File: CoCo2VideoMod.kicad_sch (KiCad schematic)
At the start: 22 parts, among them J1 Conn_01x05, J2 Conn_01x03

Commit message: circuit diagramm completed
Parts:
- added C1: 100n, symbol Device:C
- added C?: 1u, symbol Device:C
- added J3: Conn_01x06, symbol Connector_Generic:Conn_01x06
- added Q1, Q3: BC547, Package_TO_SOT_THT:TO-92_Inline, symbol Transistor_BJT:BC547
- added Q2: BC557, Package_TO_SOT_THT:TO-92_Inline, symbol Transistor_BJT:BC557
- added R? (x2): 75R, symbol Device:R
- added R? (x2): 470R, symbol Device:R
- added R?: 4k7, symbol Device:R
- added R?: 330R, symbol Device:R
- added R?: 10k, symbol Device:R
- added R?: 680R, symbol Device:R
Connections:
- net +5V: now also C1.1, Q1.1 (C), Q3.1 (C), R?.2, R?.2
- net Audio out: now also J3.1 (Pin_1)
- net GND: now also J3.3 (Pin_3), J3.4 (Pin_4), R?.1, R?.1, R?.1, R?.1
- net Luma: now also C?.2, J3.5 (Pin_5), R?.2
- net V_comp: now also J3.2 (Pin_2)
- net at R?.2, U?.8 (Co): now also Q1.2 (B)
- new net: Q1.3 (E), R?.1, R?.2
- new net: Q3.3 (E), R?.1, R?.2
- new net: C1.2, Q2.3 (E), R?.1
- new net: C?.1, Q2.2 (B), R?.1, R?.2
- new net: Q2.1 (C), Q3.2 (B), R?.2
- new net Chroma: J3.6 (Pin_6), R?.2
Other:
- moved on the sheet: C?, D?, J1, J2, L?, Q?, R?, U?

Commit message: footprint annotation
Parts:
- removed C?: 100u, symbol Device:C
- added C2: 220u, Capacitor_THT:CP_Radial_D6.3mm_P2.50mm, symbol Device:C_Polarized
- C1: value 100n -> 100p; footprint (none) -> Capacitor_THT:C_Disc_D4.7mm_W2.5mm_P5.00mm
- C3, C8: renamed from C?; footprint (none) -> Capacitor_THT:C_Rect_L7.0mm_W3.5mm_P5.00mm
- C4, C5, C7: renamed from C?; footprint (none) -> Capacitor_THT:C_Rect_L9.0mm_W4.2mm_P7.50mm_MKT
- C6: renamed from C?; footprint (none) -> Capacitor_THT:C_Rect_L7.0mm_W4.5mm_P5.00mm
- D1: renamed from D?; footprint (none) -> Diode_THT:D_DO-35_SOD27_P2.54mm_Vertical_AnodeUp
- J1: footprint (none) -> Connector_PinHeader_2.54mm:PinHeader_1x05_P2.54mm_Vertical
- J2: footprint (none) -> Connector_PinHeader_2.54mm:PinHeader_1x03_P2.54mm_Vertical
- J3: value Conn_01x06 -> Mini DIN 6p; footprint (none) -> Custom_Footprints:Connector_Mini-DIN_Female_6Pin_2rows
- L1: renamed from L?; footprint (none) -> Inductor_THT:L_Axial_L6.6mm_D2.7mm_P10.16mm_Horizontal_Vishay_IM-2
- R1, R10, R11, R12, R13, R14, R15, R16, R17, R2, R3, R4, R5, R6, R7, R8, R9: renamed from R?; footprint (none) -> Resistor_THT:R_Axial_DIN0207_L6.3mm_D2.5mm_P10.16mm_Horizontal
- U1: renamed from U?; footprint (none) -> Package_DIP:DIP-14_W7.62mm
- gave numbers to parts that had none: 2
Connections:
- net +5V: now also C2.1
- net GND: now also C2.2

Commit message: mid routing
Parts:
- removed J3: Mini DIN 6p, Custom_Footprints:Connector_Mini-DIN_Female_6Pin_2rows, symbol Connector_Generic:Conn_01x06
- added J3: Conn_01x07, Custom_Footprints:Connector_Mini-DIN_Female_6Pin_2rows, symbol Connector_Generic:Conn_01x07
- C1: footprint Capacitor_THT:C_Disc_D4.7mm_W2.5mm_P5.00mm -> Capacitor_THT:C_Disc_D3.0mm_W2.0mm_P2.50mm
- R1, R10, R11, R12, R13, R14, R15, R16, R17, R2, R3, R4, R5, R6, R7, R8, R9: footprint Resistor_THT:R_Axial_DIN0207_L6.3mm_D2.5mm_P10.16mm_Horizontal -> Resistor_THT:R_Axial_DIN0207_L6.3mm_D2.5mm_P2.54mm_Vertical
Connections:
- net Audio out: now also J3.1 (Pin_1)
- net Chroma: now also J3.6 (Pin_6)
- net GND: now also J3.3 (Pin_3), J3.4 (Pin_4), J3.7 (Pin_7)
- net Luma: now also J3.5 (Pin_5)
- net V_comp: now also J3.2 (Pin_2)

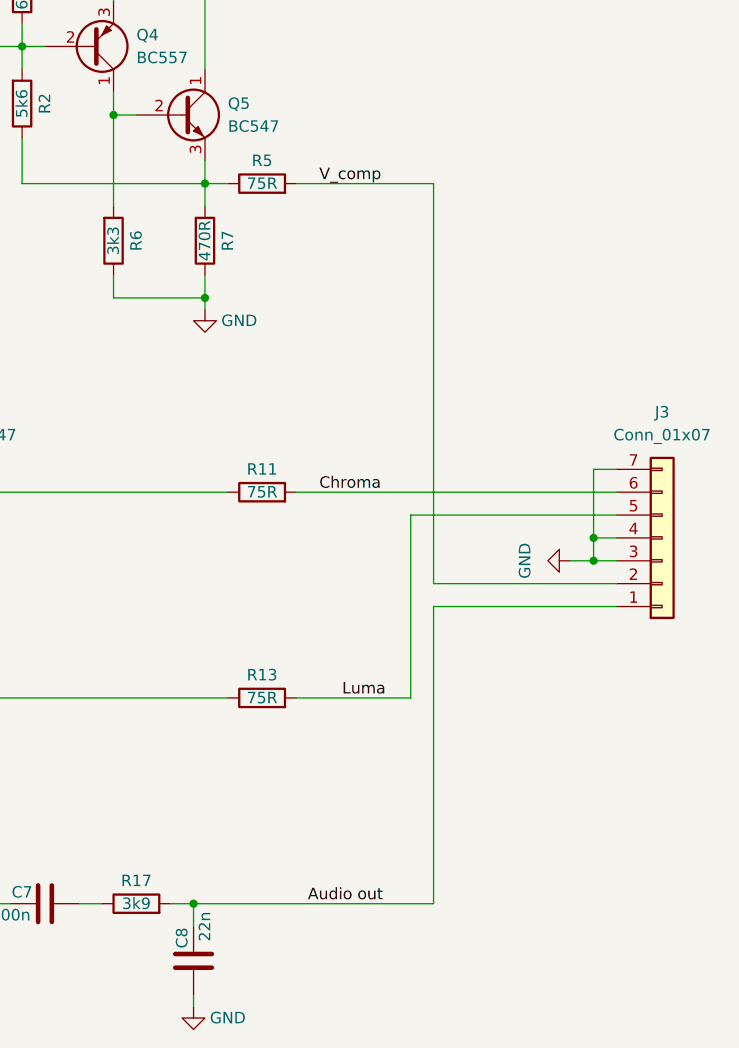
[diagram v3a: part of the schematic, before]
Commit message: midway chroma routing
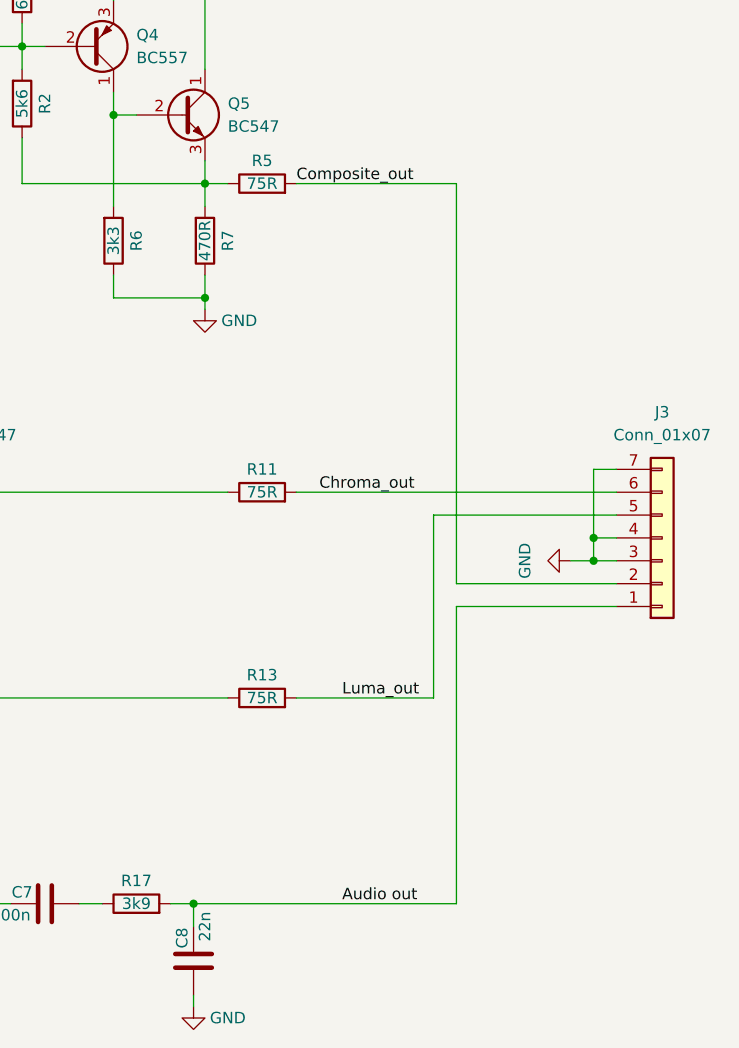
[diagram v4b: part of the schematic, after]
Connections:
- net Luma: no longer J3.5 (Pin_5), R13.2
- net Chroma renamed Chroma_out
- net V_comp renamed Composite_out
- new net Luma_out: J3.5 (Pin_5), R13.2
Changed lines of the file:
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@@
     (stroke (width 0) (type default))
   )
-  (wire (pts (xy 190.5 118.11) (xy 170.18 118.11))
+  (wire (pts (xy 190.5 118.11) (xy 172.72 118.11))
     (stroke (width 0) (type default))
   )
@@
     (stroke (width 0) (type default))
   )
-  (wire (pts (xy 143.51 151.13) (xy 170.18 151.13))
+  (wire (pts (xy 143.51 151.13) (xy 172.72 151.13))
     (stroke (width 0) (type default))
   )
@@
     (stroke (width 0) (type default))
   )
-  (wire (pts (xy 167.64 107.95) (xy 167.64 128.27))
+  (wire (pts (xy 170.18 107.95) (xy 170.18 128.27))
     (stroke (width 0) (type default))
   )
@@
     (stroke (width 0) (type default))
   )
-  (wire (pts (xy 170.18 115.57) (xy 170.18 71.12))
+  (wire (pts (xy 172.72 115.57) (xy 172.72 71.12))
     (stroke (width 0) (type default))
   )
@@
     (stroke (width 0) (type default))
   )
-  (wire (pts (xy 170.18 118.11) (xy 170.18 151.13))
+  (wire (pts (xy 172.72 118.11) (xy 172.72 151.13))
     (stroke (width 0) (type default))
   )
@@
     (stroke (width 0) (type default))
   )
-  (wire (pts (xy 154.94 71.12) (xy 170.18 71.12))
+  (wire (pts (xy 154.94 71.12) (xy 172.72 71.12))
     (stroke (width 0) (type default))
   )
@@
     (stroke (width 0) (type default))
   )
-  (wire (pts (xy 190.5 115.57) (xy 170.18 115.57))
+  (wire (pts (xy 190.5 115.57) (xy 172.72 115.57))
     (stroke (width 0) (type default))
   )
@@
     (stroke (width 0) (type default))
   )
-  (wire (pts (xy 154.94 128.27) (xy 167.64 128.27))
+  (wire (pts (xy 154.94 128.27) (xy 170.18 128.27))
     (stroke (width 0) (type default))
   )
@@
     (stroke (width 0) (type default))
   )
-  (wire (pts (xy 190.5 107.95) (xy 167.64 107.95))
+  (wire (pts (xy 190.5 107.95) (xy 170.18 107.95))
     (stroke (width 0) (type default))
   )
@@
     (effects (font (size 1.27 1.27)) (justify left bottom))
   )
-  (label "Chroma" (at 157.48 105.41 0) (fields_autoplaced)
+  (label "Chroma_out" (at 157.48 105.41 0) (fields_autoplaced)
     (effects (font (size 1.27 1.27)) (justify left bottom))
   )
@@
     (effects (font (size 1.27 1.27)) (justify left bottom))
   )
-  (label "Luma" (at 160.02 128.27 0) (fields_autoplaced)
+  (label "Luma_out" (at 160.02 128.27 0) (fields_autoplaced)
     (effects (font (size 1.27 1.27)) (justify left bottom))
   )
@@
     (effects (font (size 1.27 1.27)) (justify left bottom))
   )
-  (label "Audio out" (at 156.21 151.13 0) (fields_autoplaced)
+  (label "Audio out" (at 160.02 151.13 0) (fields_autoplaced)
     (effects (font (size 1.27 1.27)) (justify left bottom))
   )
@@
     (effects (font (size 1.27 1.27)) (justify left bottom))
   )
-  (label "V_comp" (at 157.48 71.12 0) (fields_autoplaced)
-    (effects (font (size 1.27 1.27)) (justify left bottom))
-  )
+  (label "Composite_out" (at 154.94 71.12 0) (fields_autoplaced)
+    (effects (font (size 1.27 1.27)) (justify left bottom))
+  )

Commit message: Layout complete
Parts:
- R8, R9: footprint Resistor_THT:R_Axial_DIN0207_L6.3mm_D2.5mm_P2.54mm_Vertical -> Resistor_THT:R_Axial_DIN0207_L6.3mm_D2.5mm_P7.62mm_Horizontal
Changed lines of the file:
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@@
       (effects (font (size 1.27 1.27)))
     )
-    (property "Footprint" "Resistor_THT:R_Axial_DIN0207_L6.3mm_D2.5mm_P2.54mm_Vertical" (at 91.44 88.138 90)
+    (property "Footprint" "Resistor_THT:R_Axial_DIN0207_L6.3mm_D2.5mm_P7.62mm_Horizontal" (at 91.44 88.138 90)
       (effects (font (size 1.27 1.27)) hide)
     )
@@
       (effects (font (size 1.27 1.27)))
     )
-    (property "Footprint" "Resistor_THT:R_Axial_DIN0207_L6.3mm_D2.5mm_P2.54mm_Vertical" (at 68.072 99.06 90)
-      (effects (font (size 1.27 1.27)) hide)
-    )
+    (property "Footprint" "Resistor_THT:R_Axial_DIN0207_L6.3mm_D2.5mm_P7.62mm_Horizontal" (at 68.072 99.06 90)
+      (effects (font (size 1.27 1.27)) hide)
+    )

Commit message: fab complete
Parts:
- J1: value Conn_01x05 -> 20261043
- J2: value Conn_01x03 -> to PCB
- J3: value Conn_01x07 -> Video
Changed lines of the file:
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@@
       (effects (font (size 1.27 1.27)))
     )
-    (property "Value" "Conn_01x05" (at 33.02 68.58 90)
+    (property "Value" "20261043" (at 33.02 68.58 90)
       (effects (font (size 1.27 1.27)) hide)
     )
@@
       (effects (font (size 1.27 1.27)))
     )
-    (property "Value" "Conn_01x03" (at 33.02 55.88 90)
+    (property "Value" "to PCB" (at 33.02 55.88 90)
       (effects (font (size 1.27 1.27)) hide)
     )
@@
       (effects (font (size 1.27 1.27)))
     )
-    (property "Value" "Conn_01x07" (at 195.58 99.06 0)
-      (effects (font (size 1.27 1.27)))
-    )
+    (property "Value" "Video" (at 195.58 99.06 0)
+      (effects (font (size 1.27 1.27)))
+    )

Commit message: created BOM
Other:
- company: (none) -> Riven Hexagon Electronics
- title: (none) -> TRS-80   S-Video & Composite Video Module
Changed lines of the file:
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@@
 (kicad_sch (version 20230121) (generator eeschema)
   (paper "A4")
+  (title_block
+    (title "TRS-80   S-Video & Composite Video Module")
+    (date "2023-12-01")
+    (rev "1.0")
+    (company "Riven Hexagon Electronics")
+  )
   (junction (at 80.01 140.97) (diameter 0) (color 0 0 0 0)
   )
